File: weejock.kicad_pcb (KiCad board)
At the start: 2 copper layers, 95.4 x 89.7 mm, 44 parts, among them J2 JST-PH2, K1 PG1350, K10 PG1350, K11 PG1350, K12 PG1350, K13 PG1350, K14 PG1350, K15 PG1350, K16 PG1350, K17 PG1350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

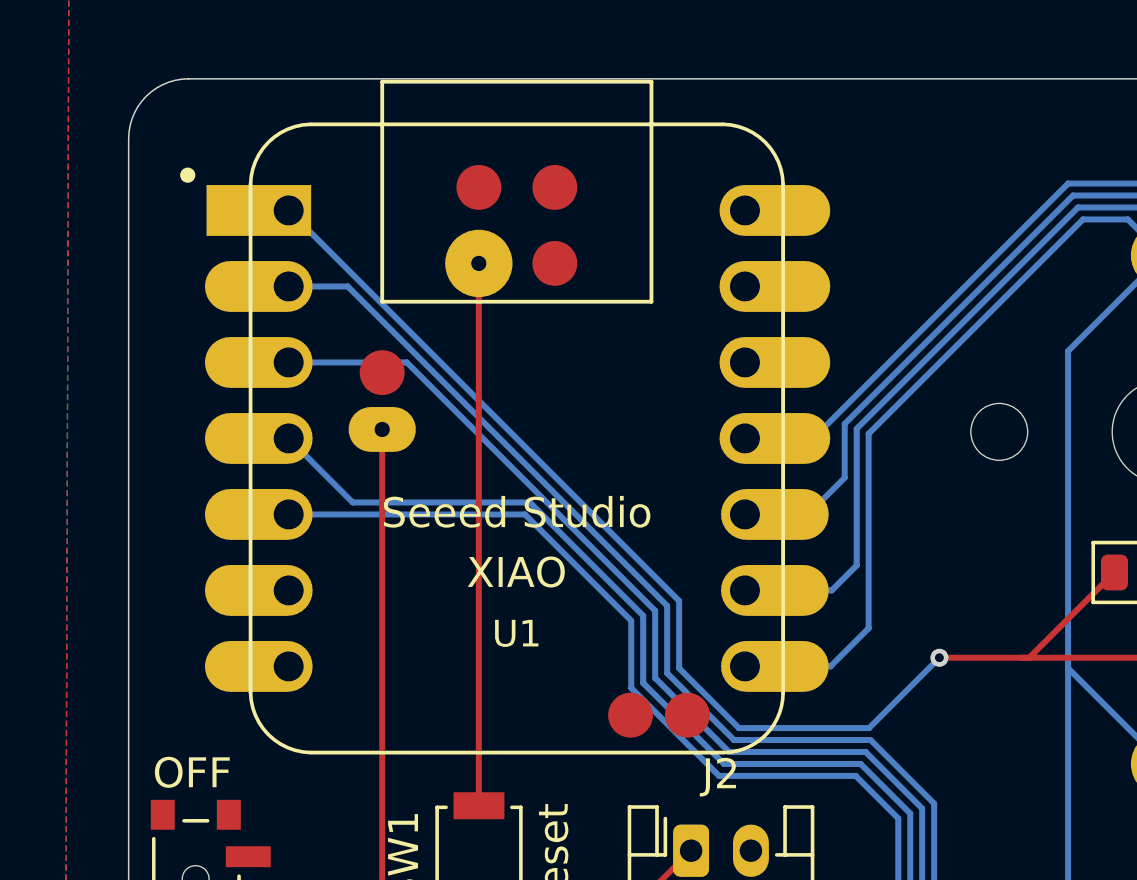
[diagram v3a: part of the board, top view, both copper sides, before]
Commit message: Pin labels for XIAO
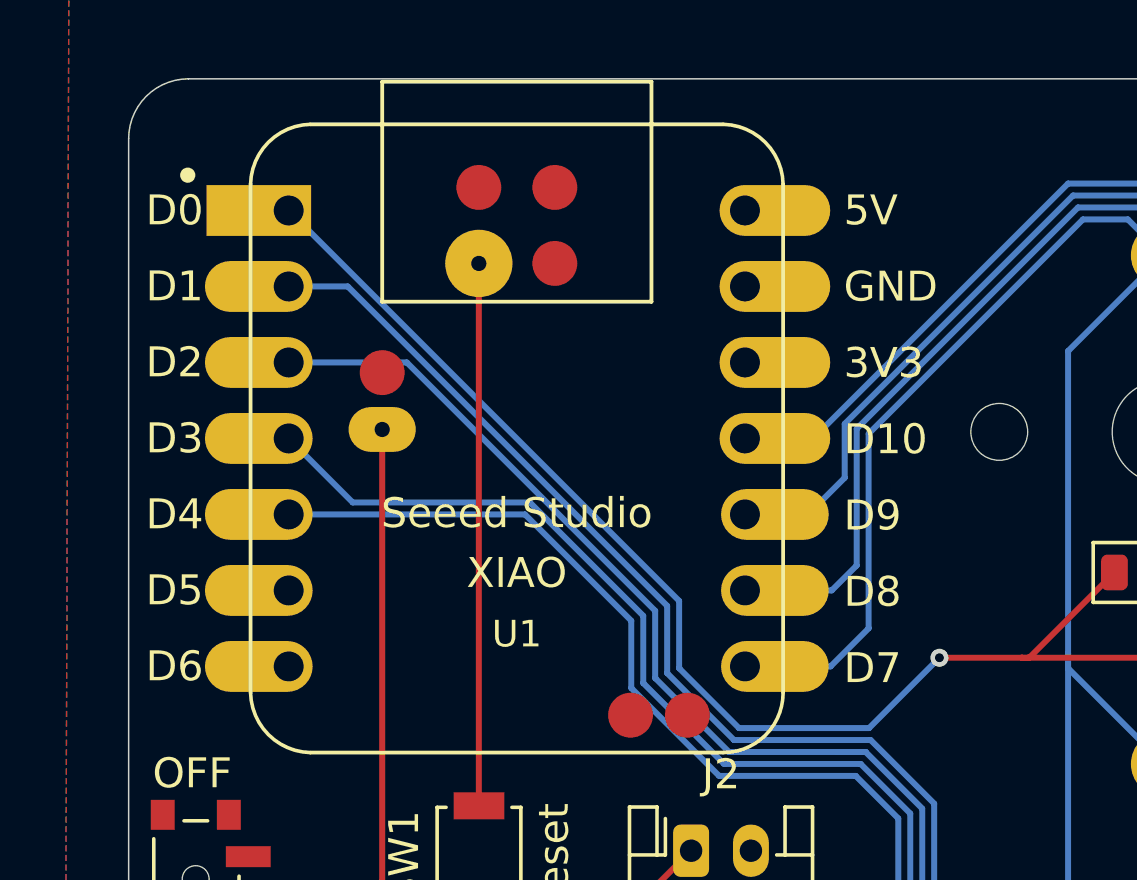
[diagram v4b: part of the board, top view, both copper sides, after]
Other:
- board text added: "3V3"
- board text added: "5V"
- board text added: "D0"
- board text added: "D1"
- board text added: "D10"
- board text added: "D2"
- board text added: "D3"
- board text added: "D4"
- board text added: "D5"
- board text added: "D6"
- board text added: "D7"
- board text added: "D8"
- board text added: "D9"
- board text added: "GND"

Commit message: More XIAO labels.
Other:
- board text added: "BAT+"
- board text added: "BAT-"
- board text added: "RST"
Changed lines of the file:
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@@
 		(fp_arc
 			(start 6.9 -10.5)
-			(mid 8.301492 -9.901492)
+			(mid 8.301494 -9.901494)
 			(end 8.9 -8.5)
 			(stroke
@@
 		)
 	)
+	(gr_text "RST"
+		(at 85 53.5 0)
+		(layer "B.SilkS")
+		(effects
+			(font
+				(size 1 1)
+				(thickness 0.1)
+			)
+			(justify left mirror)
+		)
+	)
 	(gr_text "D9"
 		(at 98.5 61.9 0)
@@
 		)
 	)
+	(gr_text "BAT+"
+		(at 84.5 59.02 0)
+		(layer "B.SilkS")
+		(effects
+			(font
+				(size 1 1)
+				(thickness 0.1)
+			)
+			(justify right mirror)
+		)
+	)
 	(gr_text "D3"
 		(at 77.1 59.32 0)
@@
 		)
 	)
+	(gr_text "RST"
+		(at 85 53.47 0)
+		(layer "F.SilkS")
+		(effects
+			(font
+				(size 1 1)
+				(thickness 0.1)
+			)
+			(justify right)
+		)
+	)
 	(gr_text "D5"
 		(at 77.1 64.4 0)
@@
 		)
 	)
+	(gr_text "BAT+"
+		(at 84.5 59.02 0)
+		(layer "F.SilkS")
+		(effects
+			(font
+				(size 1 1)
+				(thickness 0.1)
+			)
+			(justify left)
+		)
+	)
 	(gr_text "D6"
 		(at 77.1 66.94 0)
@@
 		)
 	)
+	(gr_text "BAT-"
+		(at 84.5 57.1 0)
+		(layer "F.SilkS")
+		(effects
+			(font
+				(size 1 1)
+				(thickness 0.1)
+			)
+			(justify left)
+		)
+	)
